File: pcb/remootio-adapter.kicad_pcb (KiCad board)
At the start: 2 copper layers, 105 x 60 mm, 63 parts, among them J1 AUX, J2 BATT, J3 ICSP, J4 Console, J5 SwitchIn, J6 SPM Connector, U1 remootio-3, U2 AQV252GAX, U3 LM2940S-5.0, U4 ATmega328PB-ANR, U5 ST232CDR, U6 AQV252GAX, U7 AQV252GAX, U8 AQV252GAX, Y1 CSTCE16M0V53-R0

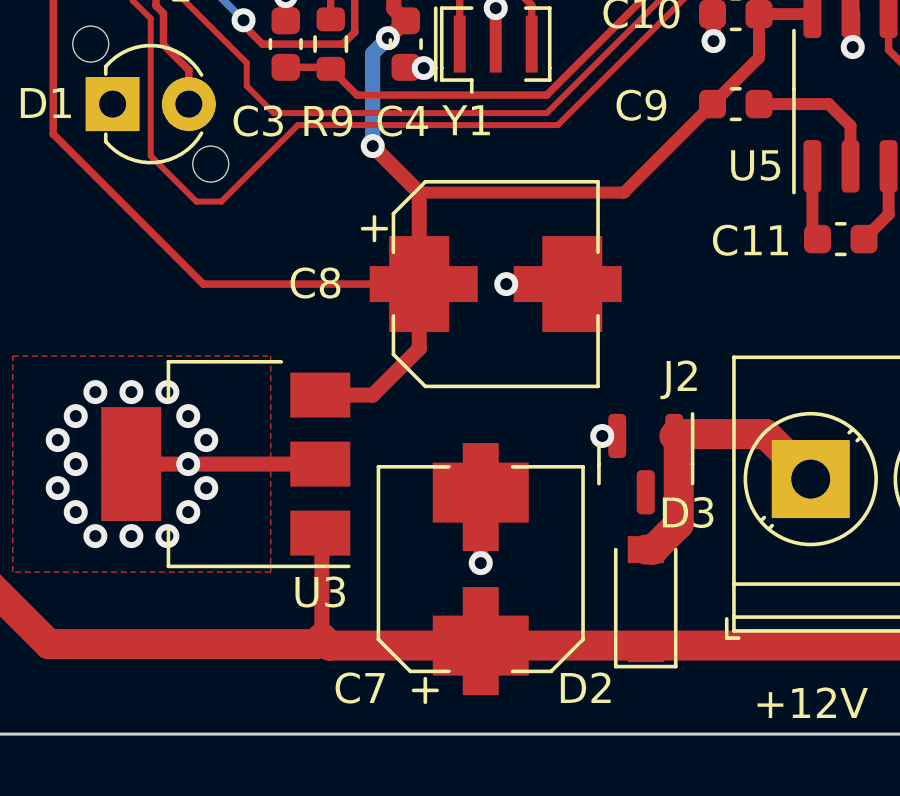
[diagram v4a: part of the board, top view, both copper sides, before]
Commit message: Replace C7 and C8 with EEEFN1V220R
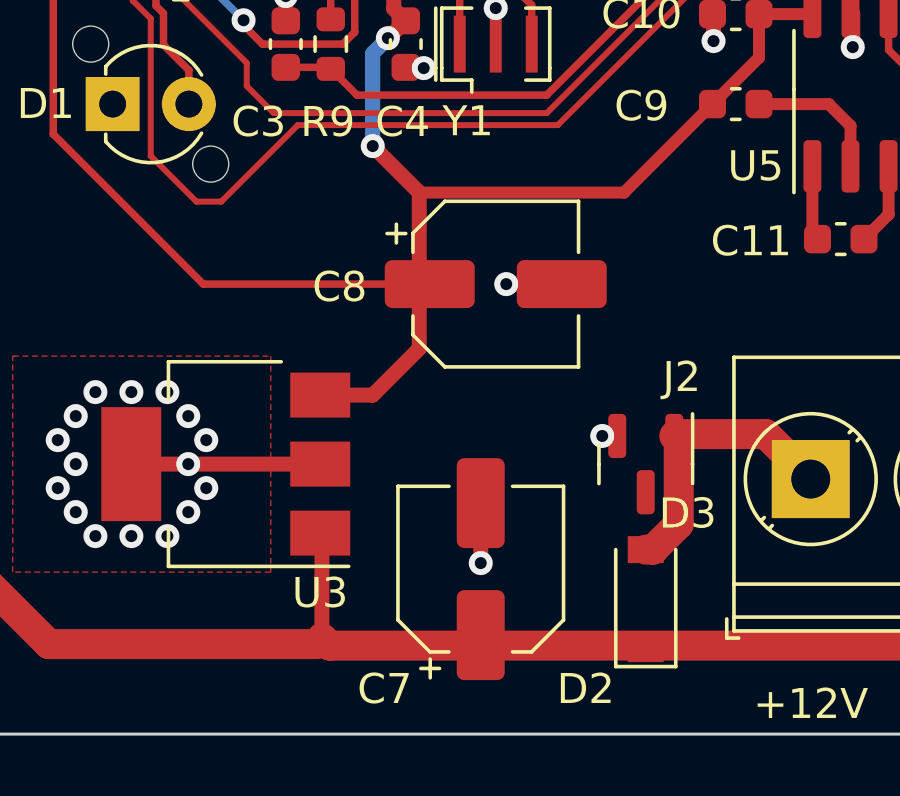
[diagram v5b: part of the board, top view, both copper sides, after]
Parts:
- C7, C8: value 22µ/63V -> 22µ/35V; footprint remootio-adapter:CP_Elec_6.3x7.7_V -> Capacitor_SMD:CP_Elec_5x5.8
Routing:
- net GND: track 38.4 -> 37.7 mm

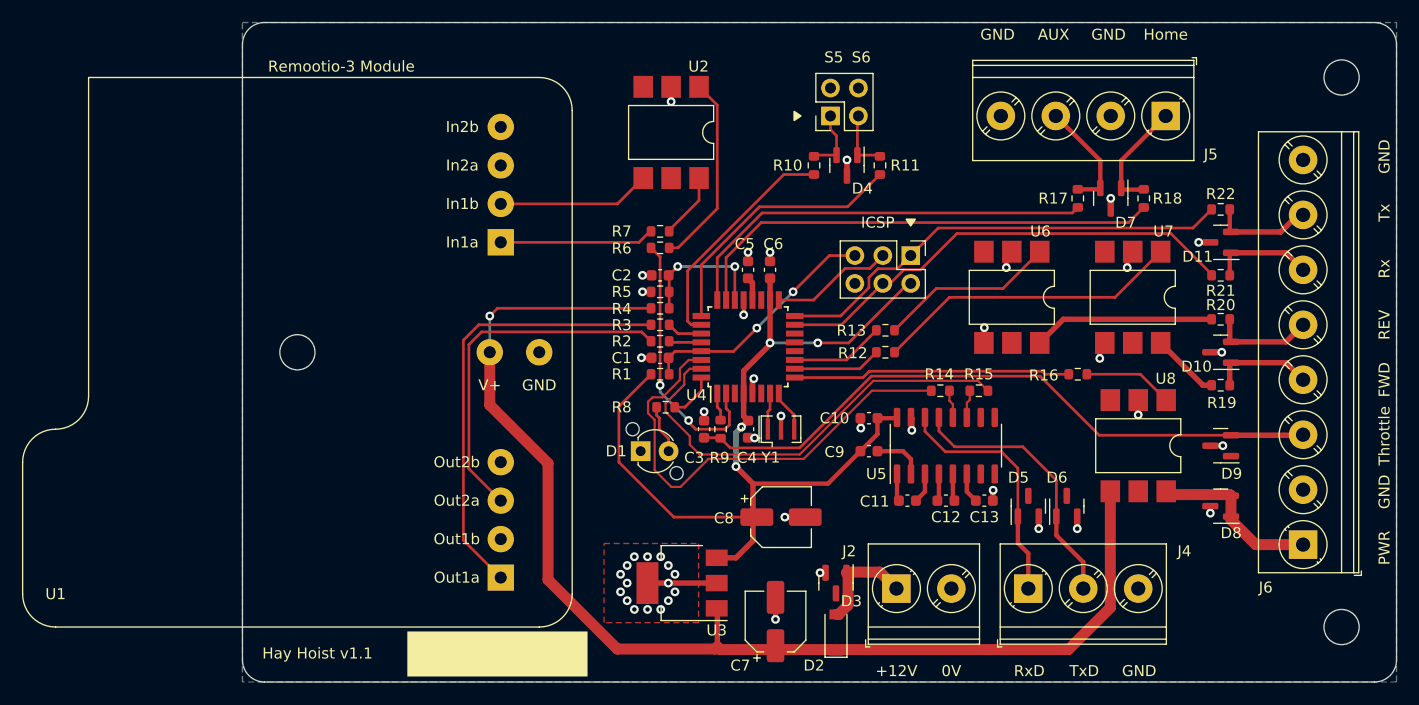
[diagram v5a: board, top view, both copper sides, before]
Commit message: Alter remootio power pads and add fiducials
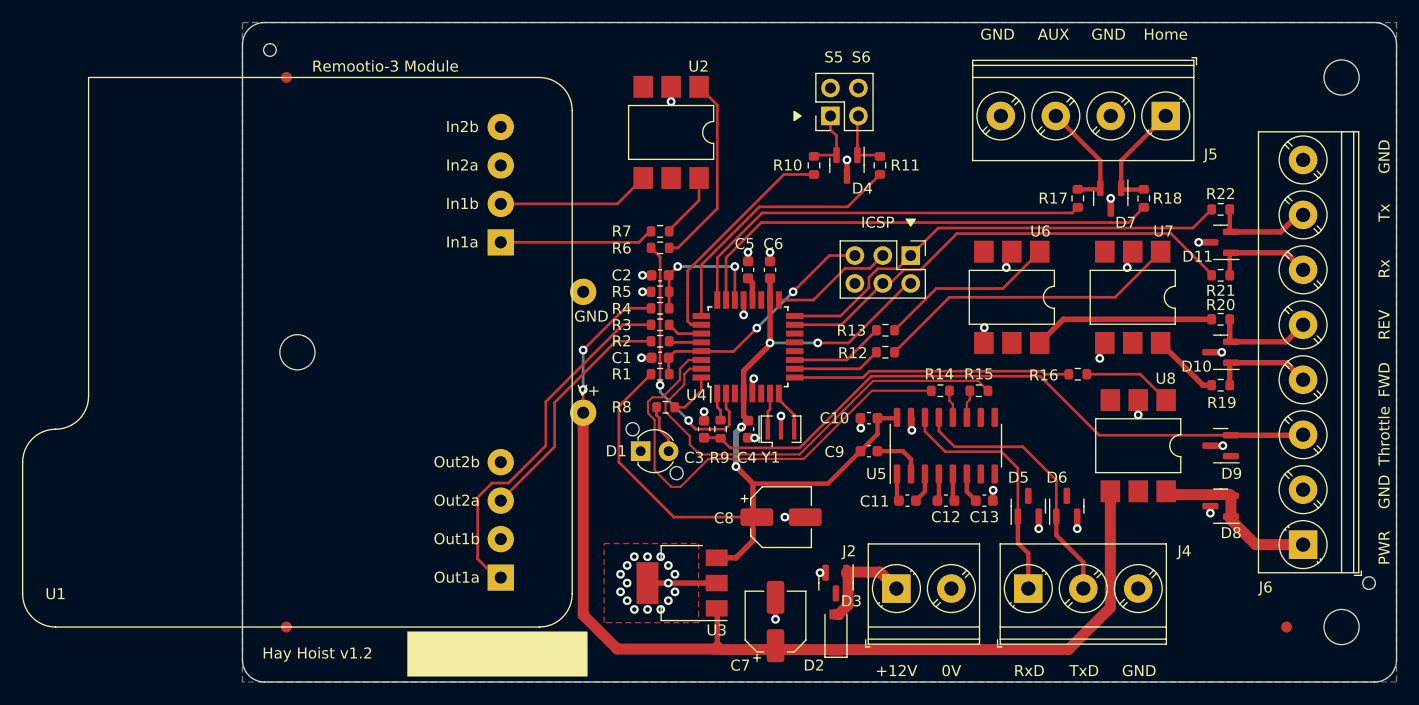
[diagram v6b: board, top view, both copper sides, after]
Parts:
- added REF**: JLCMechHole, remootio-adapter:JLCMechHole, F.Cu at (179.5, 118.0)
- added REF**: JLCMechHole, remootio-adapter:JLCMechHole, F.Cu at (79.5, 69.5)
- added REF**: Fiducial_1mm_Mask2mm, Fiducial:Fiducial_1mm_Mask2mm, F.Cu at (81.0, 72.0)
- added REF**: Fiducial_1mm_Mask2mm, Fiducial:Fiducial_1mm_Mask2mm, F.Cu at (172.0, 122.0)
- added REF**: Fiducial_1mm_Mask2mm, Fiducial:Fiducial_1mm_Mask2mm, F.Cu at (81.0, 122.0)
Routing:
- net +12V: track 110.7 -> 96.9 mm, vias 1 -> 2
- net Net-(R2-Pad1): track 32.8 -> 22.0 mm
- net Net-(R3-Pad1): track 40.7 -> 32.6 mm
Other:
- board text added: "Hay Hoist v1.2"
- board text removed: "Hay Hoist v1.1"
